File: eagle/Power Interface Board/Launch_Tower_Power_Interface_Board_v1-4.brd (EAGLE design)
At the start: 101.6 x 90.2 mm, 35 parts

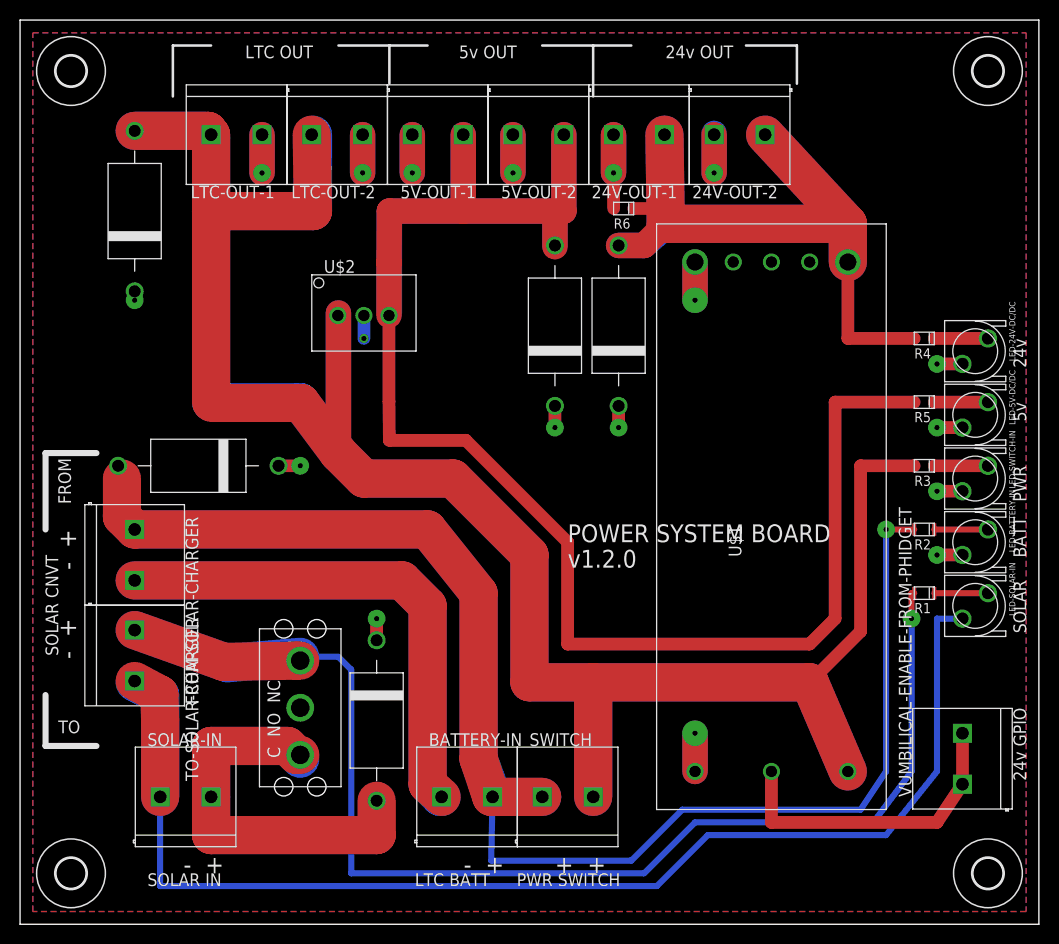
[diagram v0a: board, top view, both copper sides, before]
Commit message: Clean up of power distribution board, lots of small changes, including rcl_custom 0805 packages, ERC and DRC issues, cleaned up tnames, etc.
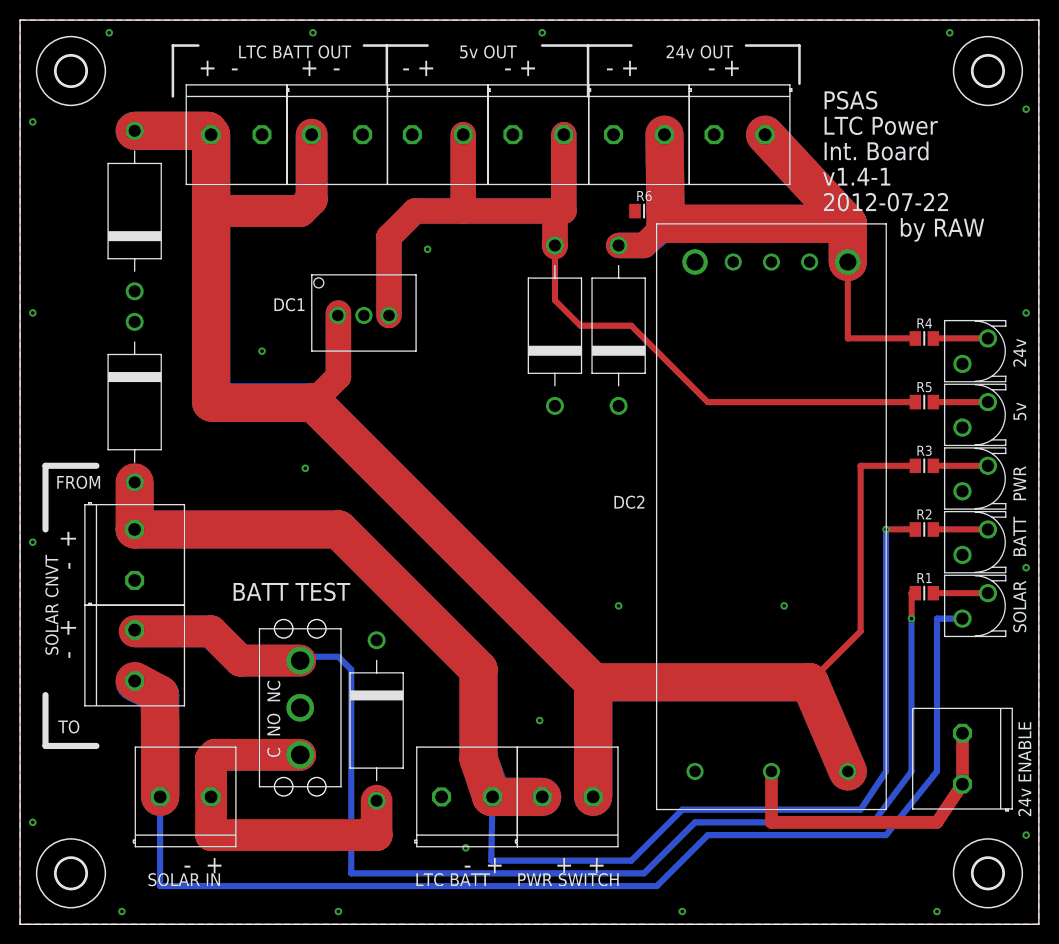
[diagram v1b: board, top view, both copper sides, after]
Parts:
- R1, R2, R3, R5: device launch-tower:0805 -> rcl_custom:0805-B
- R4: value 4.36 -> 4.36k; device launch-tower:0805 -> rcl_custom:0805-B
- R6: value (none) -> 100k; device launch-tower:0805 -> rcl_custom:0805-B
- moved ESD-BATTERYIN 8.98 mm to (11.4, 52.1), turned to 90 degrees
- moved R6 2.05 mm to (62.2, 71.1)
- renumbered U$1 to DC2, U$2 to DC1
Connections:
- net +SOLAR: now also R1.1; no longer R1.ANODE
- net GND: now also R6.1; no longer R6.ANODE
- net N$1: now also R1.2; no longer R1.CATHODE
- net N$2: now also R2.2; no longer R2.CATHODE
- net N$3: now also R3.2; no longer R3.CATHODE
- net N$4: now also R5.2; no longer R5.CATHODE
- net N$5: now also R4.2; no longer R4.CATHODE
- net V24V: now also R4.1, R6.2; no longer R4.ANODE, R6.CATHODE
- net V5V: now also R5.1; no longer R5.ANODE
- net VBAT: now also R2.1; no longer R2.ANODE
- net VLTC: now also R3.1; no longer R3.ANODE
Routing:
- net GND: track 182.7 -> 0.00 mm, vias 18 -> 23
- net V5V: track 194.6 -> 135.7 mm
- net VLTC: track 361.7 -> 336.8 mm
- net N$7: track 17.0 -> 0.00 mm
- net N$6: track 38.1 -> 49.5 mm
- net VBAT: track 208.2 -> 202.3 mm
- net N$9: track 3.81 -> 0.00 mm
- net N$8: track 3.81 -> 0.00 mm
- net V24V: track 115.0 -> 113.4 mm
- net +SOLAR: track 138.8 -> 140.3 mm
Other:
- board text added: "2012-07-22"
- board text added: "24v ENABLE"
- board text added: "BATT TEST"
- board text added: "Int. Board"
- board text added: "LTC BATT OUT"
- board text added: "LTC Power"
- board text added: "PSAS"
- board text added: "by RAW"
- board text added: "v1.4-1"
- board text removed: "24v GPIO"
- board text removed: "LTC OUT"
- board text removed: "POWER SYSTEM BOARD"
- board text removed: "v1.2.0"

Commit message: Added SPS part number to schematic and board.
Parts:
- DC2: value DC/DC_CONV_24V -> UWE-24/3-Q12P-C
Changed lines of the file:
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@@
 <?xml version="1.0" encoding="utf-8"?>
 <!DOCTYPE eagle SYSTEM "eagle.dtd">
-<eagle version="6.2">
+<eagle version="6.4">
 <drawing>
 <settings>
@@
 </class>
 </classes>
-<designrules>
+<designrules name="default">
 <description language="en">&lt;b&gt;EAGLE Design Rules&lt;/b&gt;
 &lt;p&gt;
@@
 <attribute name="VALUE" x="25.4" y="77.47" size="1.27" layer="27" rot="R180"/>
 </element>
-<element name="DC2" library="launch-tower" package="UWE" value="DC/DC_CONV_24V" x="74.93" y="40.64" smashed="yes" rot="R90">
+<element name="DC2" library="launch-tower" package="UWE" value="UWE-24/3-Q12P-C" x="74.93" y="40.64" smashed="yes" rot="R90">
 <attribute name="NAME" x="62.42" y="42.72" size="1.27" layer="25" rot="R180"/>
 </element>
